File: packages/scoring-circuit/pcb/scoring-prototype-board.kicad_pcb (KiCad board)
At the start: 2 copper layers, 160 x 100 mm, 43 parts

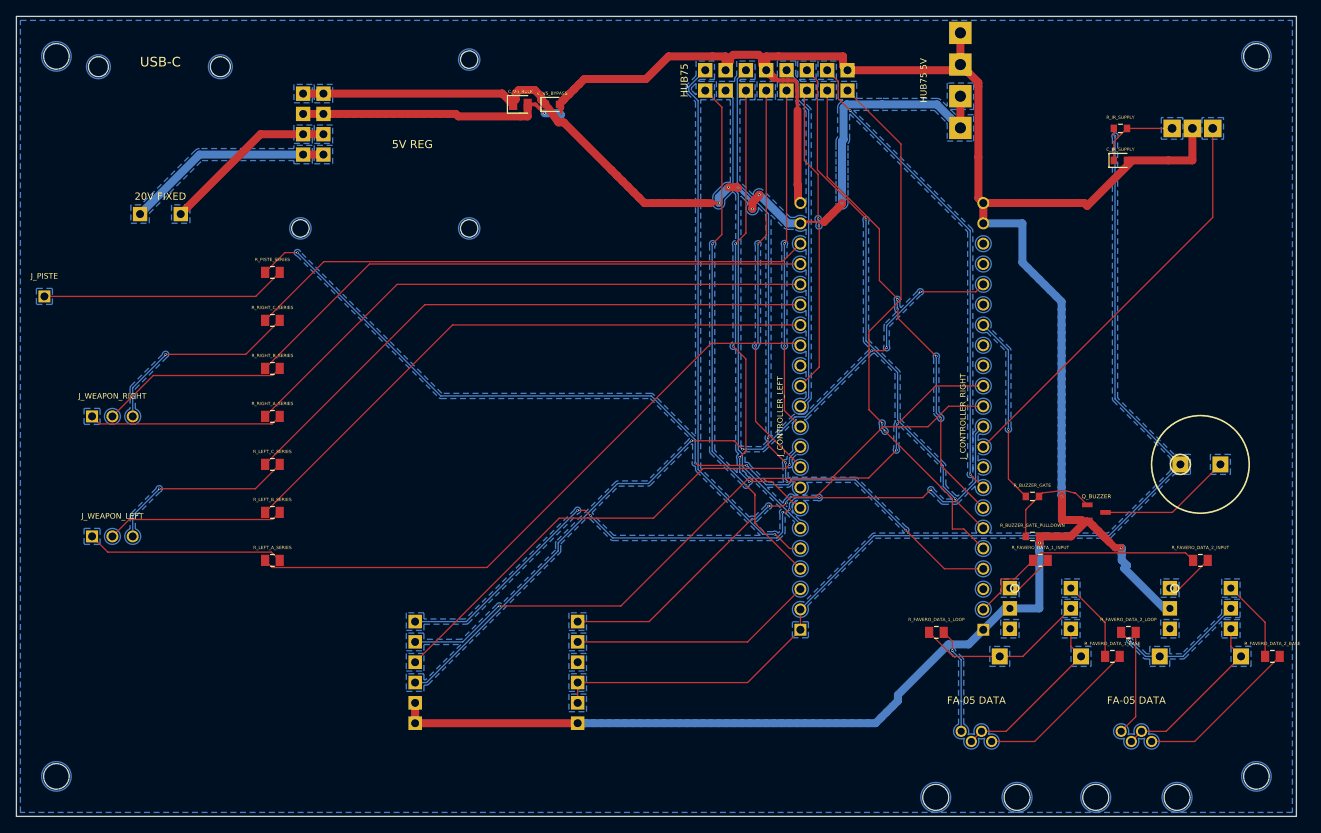
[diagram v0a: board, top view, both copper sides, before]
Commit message: feat(scoring-circuit): price the prototype order BOM
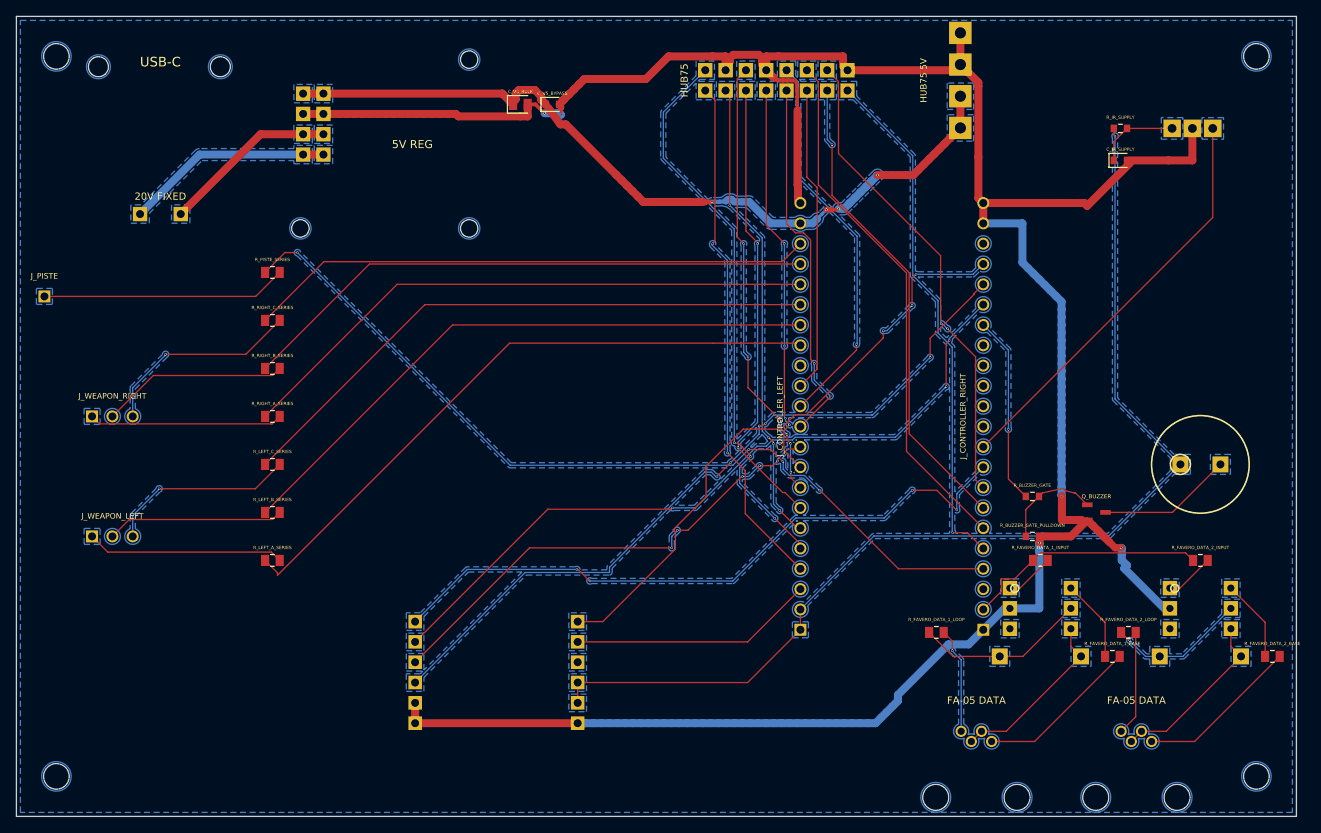
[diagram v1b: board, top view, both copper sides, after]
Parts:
- C_V5_BULK: footprint tscircuit:C2012X5R0J226M125AC -> tscircuit:C2012X5R1A226M085AC
- J_CONTROLLER_LEFT, J_CONTROLLER_RIGHT: footprint tscircuit:pin_header -> tscircuit:PPTC221LFBN-RC
- J_PISTE: footprint tscircuit:pin_header -> tscircuit:PREC001SAAN-RC
- J_WEAPON_LEFT, J_WEAPON_RIGHT: footprint tscircuit:pin_header -> tscircuit:PREC003SAAN-RC
- U_CONTROLLER_MODULE: value ESP32-S3-DevKitC-1-N8R2 -> ESP32-S3-DevKitC-1-N8R8; footprint tscircuit:ESP32-S3-DevKitC-1-N8R2 -> tscircuit:ESP32-S3-DevKitC-1-N8R8
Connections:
- J_CONTROLLER_RIGHT pad 11: ETH_INT_N -> (no net)
- J_CONTROLLER_RIGHT pad 12: ETH_CS_N -> (no net)
- J_CONTROLLER_RIGHT pad 13: APP_SPI_MISO -> (no net)
- J_CONTROLLER_RIGHT pad 17: (no net) -> ETH_CS_N
- J_CONTROLLER_RIGHT pad 19: (no net) -> APP_SPI_MISO
- J_CONTROLLER_RIGHT pad 9: (no net) -> ETH_INT_N
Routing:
- net V5: track 114.4 -> 100.7 mm, vias 6 -> 4
- net APP_SPI_MISO: track 64.8 -> 75.8 mm, vias 6 -> 3
- net ETH_CS_N: track 83.2 -> 91.8 mm, vias 1 -> 3
- net ETH_INT_N: track 90.6 -> 83.4 mm, vias 6 -> 4
- net HUB75_B: track 43.6 -> 48.6 mm, vias 0 -> 1
- net HUB75_A: track 42.9 -> 46.4 mm
- net HUB75_OE: track 68.4 -> 65.4 mm, vias 2 -> 1
- net HUB75_G1: track 68.1 -> 70.4 mm, vias 1 -> 3
- net HUB75_R2: track 58.8 -> 57.2 mm, vias 4 -> 2
- net SCORING_LEFT_A: track 79.0 -> 80.0 mm
- net HUB75_R1: track 65.7 -> 65.0 mm
- net HUB75_G2: track 56.5 -> 55.9 mm, vias 3 -> 6
- net HUB75_B2: track 50.0 -> 49.4 mm, vias 2 -> 4
- net APP_SPI_SCK: track 59.8 -> 60.3 mm, vias 1 -> 6
- net HUB75_C: track 38.8 -> 38.3 mm, vias 2 -> 0
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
